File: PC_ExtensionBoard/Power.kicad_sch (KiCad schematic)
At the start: 73 parts, among them J4 Conn_01x02_Socket, J5 Conn_01x02_Socket, Q3 BSS138-7-F, Q4 SI7613DN-T1-GE3, SW1 K2-1808SN-A4SW, SW2 K2-1808SN-A4SW, U19 TPS56C230, U20 TPS3840PL30DBVR, U21 TPS564247DRLR, U23 TLV73333PDBVT, U49 INA219AIDCNR, U50 INA219AIDCNR, U9 CH224K

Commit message: update LCSC Number
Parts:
- removed DC1: DC-044A-20A, ACLAB:DC-IN-TH_DC-044A-20A, symbol A_PC_ExtensionBoard:DC-044A-20A_
- added U12: DC-528φ2.0(HY), PC_Components_1:DC-IN-TH_DC-528-2.0-HY, symbol A_PC_ExtensionBoard:DC-528φ2.0(HY)
- BT1: LCSC (none) -> C5359599
- C39: footprint antmicro-footprints:C_Pol_EIA-D -> PC_Components_1:CAP-SMD_L7.3-W4.3-R-RD; LCSC (none) -> C147770
- C40, C58, C59: footprint antmicro-footprints:C_0603_1608Metric -> PC_Components_1:C_0603_1608Metric; LCSC (none) -> C2762594
- C45, C50, C62: footprint antmicro-footprints:C_0402_1005Metric -> PC_Components_1:C_0402_1005Metric; LCSC (none) -> C2182694
- C48: footprint antmicro-footprints:C_0402_1005Metric -> PC_Components_1:C_0402_1005Metric
- C52, C64: footprint antmicro-footprints:C_Pol_EIA-B -> PC_Components_1:CAP-SMD_L3.5-W2.8; LCSC (none) -> C600583
- C57, C61, C66, C67, C69, C70: LCSC (none) -> C2182694
- J4, J5: LCSC (none) -> C18077890
- L3: LCSC (none) -> C20636406
- R37: LCSC (none) -> C202396
- R40: LCSC (none) -> C202394
- R47: LCSC (none) -> C138026
- R86: Author Antmicro -> (none); LCSC (none) -> C202396; License Apache-2.0 -> (none); MPN CR0402-FX-1002GLF -> (none); Manufacturer Bourns -> (none); Public False -> (none)
- U9: footprint PC_ExtensionBoard:ESSOP-10_L4.9-W3.9-P1.0-LS6.0-TL-EP -> PC_Components_1:ESSOP-10_L4.9-W3.9-P1.0-LS6.0-TL-EP
- USBC1: LCSC (none) -> C165948
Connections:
- net +12V: now also U12.4
- net GND: now also U9.11 (GND), U12.1, U12.2, U12.3, U12.5, U12.6; no longer U9.0 (GND)

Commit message: update Schematic
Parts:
- added R103: R_0R_0402, PC_Components_1:R_0402_1005Metric, symbol A_PC_ExtensionBoard:R_0R_0402
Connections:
- net PWR_OK: now also R103.2; no longer R105.2, U20.1 (~{RESET})
- new net: R103.1, R105.2, U20.1 (~{RESET})
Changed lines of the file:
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@@
 	)
 	(junction
+		(at 382.27 143.51)
+		(diameter 0)
+		(color 0 0 0 0)
+	)
+	(junction
 		(at 281.94 149.86)
 		(diameter 0)
@@
 	)
 	(junction
-		(at 382.27 143.51)
-		(diameter 0)
-		(color 0 0 0 0)
-	)
-	(junction
 		(at 353.06 55.88)
 		(diameter 0)
@@
 	(wire
 		(pts
-			(xy 386.08 143.51) (xy 382.27 143.51)
-		)
-		(stroke
-			(width 0)
-			(type default)
-		)
-	)
-	(wire
-		(pts
 			(xy 532.13 217.17) (xy 534.67 217.17)
 		)
@@
 	(wire
 		(pts
+			(xy 382.27 138.43) (xy 382.27 135.89)
+		)
+		(stroke
+			(width 0)
+			(type default)
+		)
+	)
+	(wire
+		(pts
 			(xy 370.84 55.88) (xy 370.84 76.2)
 		)
@@
 	(wire
 		(pts
+			(xy 382.27 135.89) (xy 383.54 135.89)
+		)
+		(stroke
+			(width 0)
+			(type default)
+		)
+	)
+	(wire
+		(pts
 			(xy 355.6 130.81) (xy 347.98 130.81)
 		)
@@
 	(hierarchical_label "PWR_OK"
 		(shape output)
-		(at 386.08 143.51 0)
+		(at 383.54 135.89 0)
 		(effects
 			(font
@@
 					(unit 1)
 				)
+			)
+		)
+	)
+	(symbol
+		(lib_id "A_PC_ExtensionBoard:R_0R_0402")
+		(at 382.27 143.51 90)
+		(unit 1)
+		(body_style 1)
+		(exclude_from_sim no)
+		(in_bom yes)
+		(on_board yes)
+		(in_pos_files yes)
+		(dnp no)
+		(property "Reference" "R103"
+			(at 378.968 140.462 0)
+			(show_name no)
+			(do_not_autoplace no)
+			(effects
+				(font
+					(size 1.27 1.27)
+					(thickness 0.15)
+				)
+			)
+		)
+		(property "Value" "R_0R_0402"
+			(at 394.97 123.19 0)
+			(hide yes)
+			(show_name no)
+			(do_not_autoplace no)
+			(effects
+				(font
+					(size 1.27 1.27)
+					(thickness 0.15)
+				)
+				(justify left bottom)
+			)
+		)
+		(property "Footprint" "PC_Components_1:R_0402_1005Metric"
+			(at 397.51 123.19 0)
+			(hide yes)
+			(show_name no)
+			(do_not_autoplace no)
+			(effects
+				(font
+					(size 1.27 1.27)
+					(thickness 0.15)
+				)
+				(justify left bottom)
+			)
+		)
+		(property "Datasheet" "https://industrial.panasonic.com/cdbs/www-data/pdf/RDA0000/AOA0000C301.pdf"
+			(at 400.05 123.19 0)
+			(hide yes)
+			(show_name no)
+			(do_not_autoplace no)
+			(effects
+				(font
+					(size 1.27 1.27)
+					(thickness 0.15)
+				)
+				(justify left bottom)
+			)
+		)
+		(property "Description" ""
+			(at 382.27 143.51 0)
+			(hide yes)
+			(show_name no)
+			(do_not_autoplace no)
+			(effects
+				(font
+					(size 1.27 1.27)
+				)
+			)
+		)
+		(property "MPN" "ERJ2GE0R00X"
+			(at 402.59 123.19 0)
+			(hide yes)
+			(show_name no)
+			(do_not_autoplace no)
+			(effects
+				(font
+					(size 1.27 1.27)
+					(thickness 0.15)
+				)
+				(justify left bottom)
+			)
+		)
+		(property "Manufacturer" "Panasonic"
+			(at 405.13 123.19 0)
+			(hide yes)
+			(show_name no)
+			(do_not_autoplace no)
+			(effects
+				(font
+					(size 1.27 1.27)
+					(thickness 0.15)
+				)
+				(justify left bottom)
+			)
+		)
+		(property "License" "Apache-2.0"
+			(at 407.67 123.19 0)
+			(hide yes)
+			(show_name no)
+			(do_not_autoplace no)
+			(effects
+				(font
+					(size 1.27 1.27)
+					(thickness 0.15)
+				)
+				(justify left bottom)
+			)
+		)
+		(property "Author" "Antmicro"
+			(at 410.21 123.19 0)
+			(hide yes)
+			(show_name no)
+			(do_not_autoplace no)
+			(effects
+				(font
+					(size 1.27 1.27)
+					(thickness 0.15)
+				)
+				(justify left bottom)
+			)
+		)
+		(property "Val" "0R"
+			(at 379.222 136.144 0)
+			(show_name no)
+			(do_not_autoplace no)
+			(effects
+				(font
+					(size 1.27 1.27)
+					(thickness 0.15)
+				)
+			)
+		)
+		(property "Tolerance" ""
+			(at 392.43 123.19 0)
+			(hide yes)
+			(show_name no)
+			(do_not_autoplace no)
+			(effects
+				(font
+					(size 1.27 1.27)
+				)
+				(justify left bottom)
+			)
+		)
+		(property "Current" "1A"
+			(at 412.75 123.19 0)
+			(hide yes)
+			(show_name no)
+			(do_not_autoplace no)
+			(effects
+				(font
+					(size 1.27 1.27)
+					(thickness 0.15)
+				)
+				(justify left bottom)
+			)
+		)
+		(property "Public" "False"
+			(at 412.75 123.19 0)
+			(hide yes)
+			(show_name no)
+			(do_not_autoplace no)
+			(effects
+				(font
+					(size 1.27 1.27)
+				)
+				(justify left bottom)
+			)
+		)
+		(pin "2"
+		)
+		(pin "1"
+		)
+		(instances
+			(project "PC_ExtensionBoard"
+				(path "/6f8c8ec7-fa36-4248-8716-390866a3d0b0/d5783b1a-f6ab-498c-a6d2-017d56dd6434"
+					(reference "R103")
+					(unit 1)
+				)

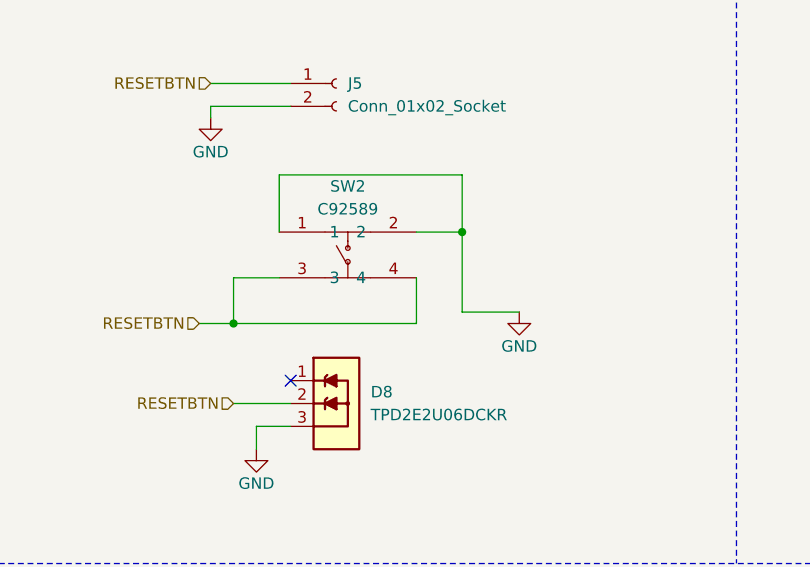
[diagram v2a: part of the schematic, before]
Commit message: finished highspeed routing
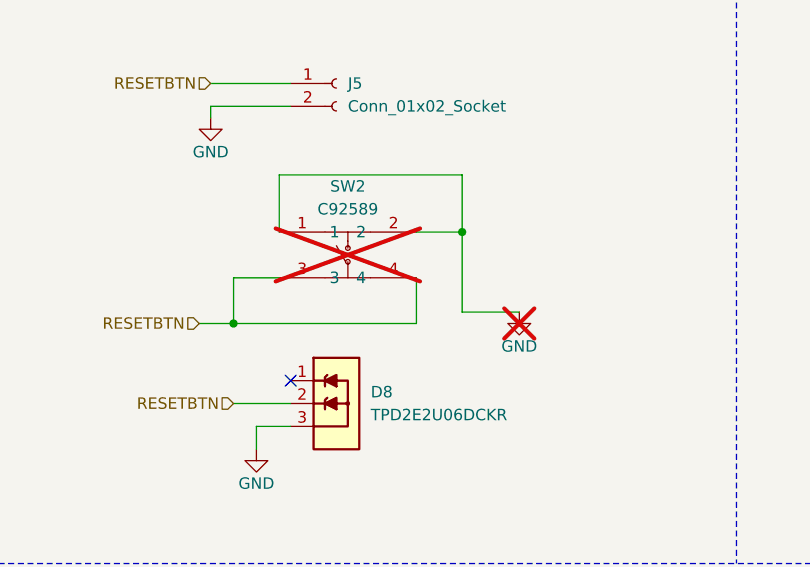
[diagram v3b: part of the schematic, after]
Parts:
- J4, J5: footprint PC_Components_1:CONN-SMD_2P-P2.00_BX-PH2.0-2PWT -> Connector_PinHeader_2.00mm:PinHeader_1x02_P2.00mm_Vertical
- SW2: now not fitted; now left out of the parts list
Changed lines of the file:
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@@
 			)
 		)
-		(property "Footprint" "PC_Components_1:CONN-SMD_2P-P2.00_BX-PH2.0-2PWT"
+		(property "Footprint" "Connector_PinHeader_2.00mm:PinHeader_1x02_P2.00mm_Vertical"
 			(at 267.97 209.55 0)
 			(hide yes)
@@
 		(body_style 1)
 		(exclude_from_sim no)
-		(in_bom yes)
-		(on_board yes)
+		(in_bom no)
+		(on_board no)
 		(in_pos_files yes)
-		(dnp no)
+		(dnp yes)
 		(property "Reference" "#PWR0453"
 			(at 297.18 237.49 0)
@@
 			)
 		)
-		(property "Footprint" "PC_Components_1:CONN-SMD_2P-P2.00_BX-PH2.0-2PWT"
+		(property "Footprint" "Connector_PinHeader_2.00mm:PinHeader_1x02_P2.00mm_Vertical"
 			(at 356.87 203.2 0)
 			(hide yes)
@@
 		(body_style 1)
 		(exclude_from_sim no)
-		(in_bom yes)
-		(on_board yes)
+		(in_bom no)
+		(on_board no)
 		(in_pos_files yes)
-		(dnp no)
+		(dnp yes)
 		(fields_autoplaced yes)
 		(property "Reference" "SW2"

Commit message: bug fixes
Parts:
- BT1: LCSC C5359599 -> (none)
- J4, J5: LCSC C18077890 -> (none)
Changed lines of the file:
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@@
 			)
 		)
-		(property "LCSC" "C5359599"
-			(at 562.61 297.18 0)
-			(hide yes)
-			(show_name no)
-			(do_not_autoplace no)
-			(effects
-				(font
-					(size 1.27 1.27)
-				)
-			)
-		)
 		(pin "1"
 		)
@@
 			)
 		)
-		(property "LCSC" "C18077890"
-			(at 267.97 209.55 0)
-			(hide yes)
-			(show_name no)
-			(do_not_autoplace no)
-			(effects
-				(font
-					(size 1.27 1.27)
-				)
-			)
-		)
 		(pin "2"
 		)
@@
 			(at 356.87 203.2 0)
 			(hide yes)
-			(show_name no)
-			(do_not_autoplace no)
-			(effects
-				(font
-					(size 1.27 1.27)
-				)
-			)
-		)
-		(property "LCSC" "C18077890"
-			(at 356.87 203.2 0)
-			(hide yes)
